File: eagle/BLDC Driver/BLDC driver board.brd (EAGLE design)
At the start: 59.7 x 47 mm, 25 parts, among them Q1 MOSFET-NCHANNEL, Q2 MOSFET-NCHANNEL, Q3 MOSFET-NCHANNEL, Q4 MOSFET-NCHANNEL, Q5 MOSFET-NCHANNEL, Q6 MOSFET-NCHANNEL, U2 AUIRS2334S

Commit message: Started working on new driver board.
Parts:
- removed D1, D2, D6: (no value), CMPE118lib:DIODE-HV
- removed U2: AUIRS2334S, ASL:SO20W
- added 5V: (no value), jumper:JP1
- added C5, C6, R2: (no value), ASL:0805
- added U$2: DRV8302, ASL:SOP63P1035X279-56N
- C1: value 470nF -> .1uF; device CMPE118lib:1206 -> ASL:0805
- C2: value 470nF -> 4.7uF; device CMPE118lib:1206 -> ASL:0805
- C3: value 470nF -> .015uF; device CMPE118lib:1206 -> ASL:0805
- C4: value 1uF -> (none); device CMPE118lib:1206 -> ASL:0805
- moved C4 80.9 mm to (-17.8, -30.5), turned to 0 degrees
- moved C3 70.8 mm to (-17.8, -20.3)
- moved C2 59.5 mm to (-17.8, -10.2)
- moved C1 52.6 mm to (-17.8, -5.08)
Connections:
- removed net N$11: C3.1, D6.C, U2.14
- new net CRRNTSNS1: U$1.P$21
- new net CRRNTSNS2: U$1.P$4
- new net N$1: C3.2, U$2.56
- new net N$4: C4.1, U$2.48
- new net N$5: C4.2, U$2.46
- new net N$6: C5.1, U$2.43
- new net N$8: C6.1, U$2.38
- new net N$9: C6.2, U$2.36
- new net PGND: Q2.3, Q4.3, Q6.3, U$2.P$1
- new net PVDD: C1.1, C2.1, Q1.4, Q1.4@1, Q1.P$2, Q1.P$3, Q1.P$4, Q1.P$5, Q1.P$6, Q1.P$7, Q1.P$8, Q1.P$9, Q3.4, Q3.4@1, Q3.P$2, Q3.P$3, Q3.P$4, Q3.P$5, Q3.P$6, Q3.P$7, Q3.P$8, Q3.P$9, Q5.4, Q5.4@1, Q5.P$2, Q5.P$3, Q5.P$4, Q5.P$5, Q5.P$6, Q5.P$7, Q5.P$8, Q5.P$9, U$2.29, U$2.53, U$2.54
- net +UB: no longer Q1.4, Q1.4@1, Q1.P$2, Q1.P$3, Q1.P$4, Q1.P$5, Q1.P$6, Q1.P$7, Q1.P$8, Q1.P$9, Q3.4, Q3.4@1, Q3.P$2, Q3.P$3, Q3.P$4, Q3.P$5, Q3.P$6, Q3.P$7, Q3.P$8, Q3.P$9, Q5.4, Q5.4@1, Q5.P$2, Q5.P$3, Q5.P$4, Q5.P$5, Q5.P$6, Q5.P$7, Q5.P$8, Q5.P$9
- net -UB: no longer Q2.3, Q4.3, Q6.3
- net GND: now also 5V.1, C1.2, C2.2, C3.1, R2.2; no longer C4.2, U2.7
- net HO1: no longer U2.19
- net HO2: no longer U2.16
- net HO3: no longer U2.13
- net LO1: no longer U2.10
- net LO2: no longer U2.9
- net LO3: no longer U2.8
- net N$3: now also R2.1, U$2.49; no longer C1.1, D1.C, U2.20
- net N$7: now also C5.2, U$2.41; no longer C2.1, D2.C, U2.17
- net OUTPUTA: no longer C1.2, U2.18
- net OUTPUTB: no longer C2.2, U2.15
- net OUTPUTC: no longer C3.2, U2.12
- net PWM1: now also U$2.17; no longer U2.1, U2.4
- net PWM2: now also U$2.19; no longer U2.2, U2.5
- net PWM3: now also U$2.21; no longer U2.3, U2.6
- net VCC: now also 5V.2; no longer C4.1, D1.A, D2.A, D6.A, U2.11
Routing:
- net OUTPUTB: track 159.1 -> 0.00 mm, vias 4 -> 0
- net OUTPUTA: track 134.1 -> 0.00 mm, vias 1 -> 0
- net HO2: track 115.8 -> 0.00 mm, vias 4 -> 0
- net OUTPUTC: track 100.6 -> 0.00 mm, vias 4 -> 0
- net LO3: track 86.0 -> 0.00 mm
- net LO1: track 75.3 -> 0.00 mm, vias 2 -> 0
- net LO2: track 65.8 -> 0.00 mm
- net VCC: track 65.3 -> 0.00 mm
- net PWM2: track 55.6 -> 0.00 mm, vias 3 -> 0
- net PWM3: track 54.0 -> 0.00 mm, vias 3 -> 0
- net PWM1: track 52.3 -> 0.00 mm, vias 1 -> 0
- net HO1: track 51.7 -> 0.00 mm, vias 2 -> 0
- net HO3: track 40.7 -> 0.00 mm, vias 2 -> 0
- net ADC/HALL1: track 34.9 -> 0.00 mm, vias 2 -> 0
- net N$11: track 27.5 -> 0.00 mm, vias 2 -> 0
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- removed copper zone on layer 1, net +UB
- removed copper zone on layer 16, net +UB
- removed copper zone on layer 1, net -UB
- removed copper zone on layer 16, net -UB
- removed copper zone on layer 1, net GND

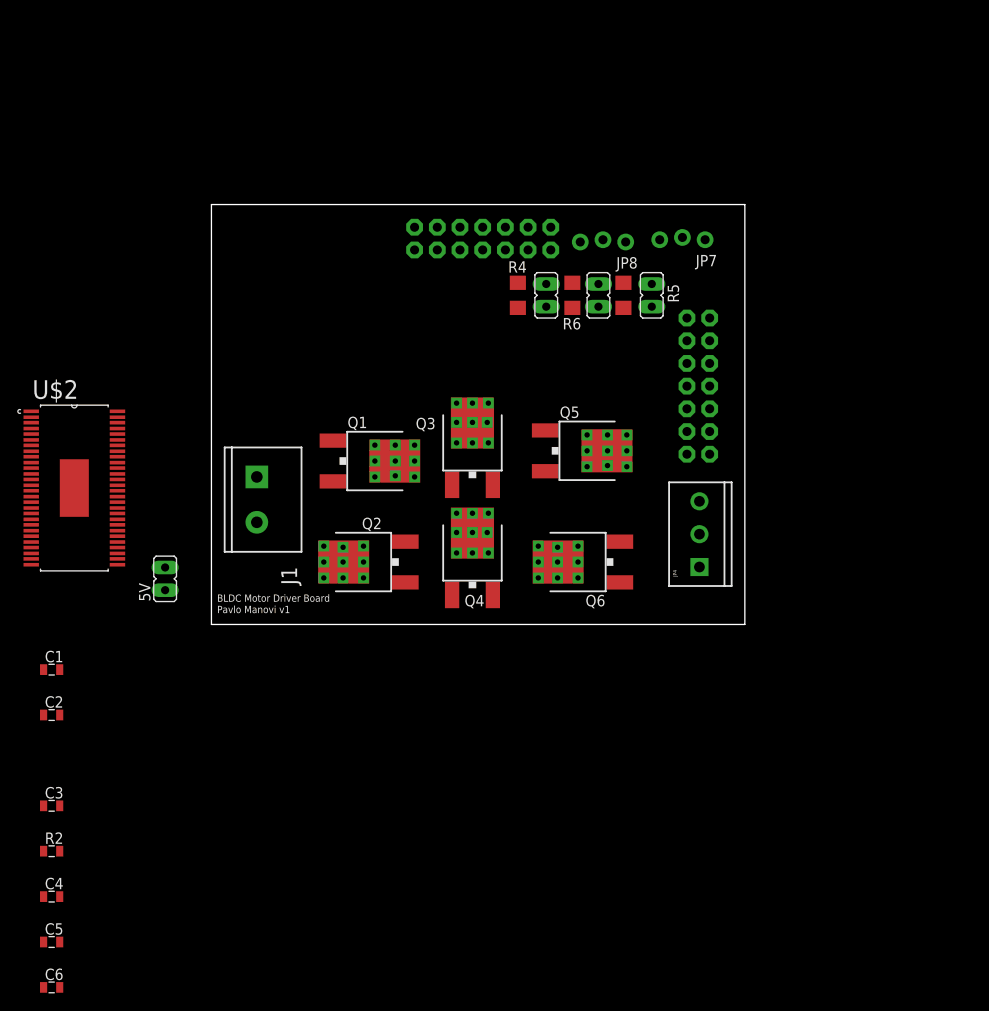
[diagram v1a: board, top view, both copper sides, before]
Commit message: Finished BLDC Driver v2.1
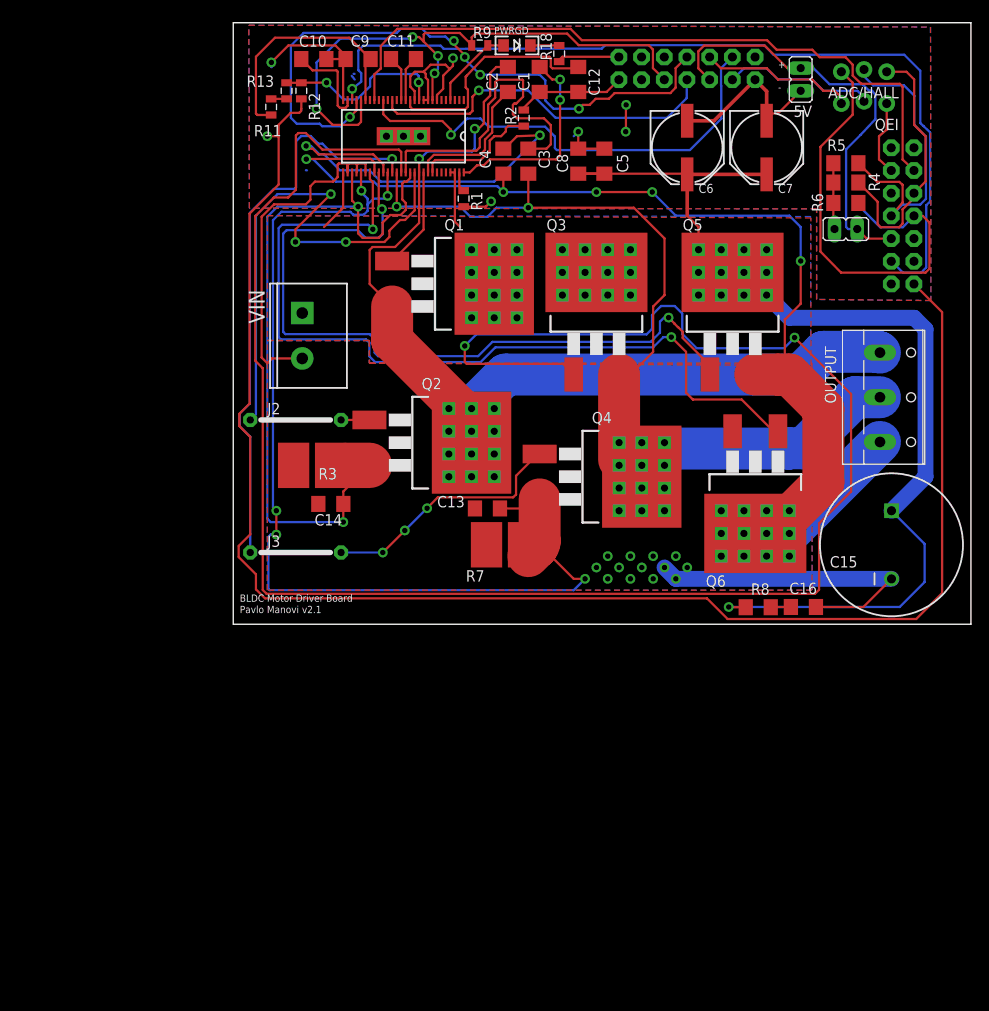
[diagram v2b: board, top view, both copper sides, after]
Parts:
- removed J1: (no value), CMPE118lib:SCREW_TERMINAL-5.08MM-2
- removed JP1, JP2: (no value), jumper:JP1
- removed JP4: (no value), CMPE118lib:SCREWTERMINAL-3.5MM-3_LOCK.007S
- removed JP7, JP8: (no value), CMPE118lib:1X03_LOCK_NO_SILK
- removed U$2: DRV8302, ASL:SOP63P1035X279-56N
- added ADC/HALL, QEI: (no value), CMPE118lib:1X03_LOCK_NO_SILK
- added C10, C9: 1uF, ASL:1206
- added C11: 22nF, ASL:1206
- added C12: 2.2uF, ASL:1206
- added C13, C14: 1nF, ASL:1206
- added C15: 470, ASL:CPOL-RADIAL-1000UF-63V
- added C16: 10nF, ASL:1206
- added C7: 4.7uF, ASL:PANASONIC_E
- added C8: .1uF, ASL:1206
- added DRV8301: DRV8302, ASL:HTSSOP56
- added J2, J3: J10MM, jumper:10
- added LED3: (no value), ASL:LED-1206
- added OUTPUT: (no value), con-wago-500:W237-103
- added R1, R11, R9: 10k, ASL:0805
- added R12: 3.16, ASL:0805
- added R13: 470, ASL:0805
- added R18: 330, ASL:0805
- added R3, R7: .01, ASL:SMT-REF
- added R8: 3.3, CMPE118lib:1206
- added VIN: (no value), CMPE118lib:SCREW_TERMINAL-5.08MM-2
- C1: value .1uF -> .015uF; device ASL:0805 -> ASL:1206
- C2: value 4.7uF -> .1uF; device ASL:0805 -> ASL:1206
- C3: value .015uF -> .1uF; device ASL:0805 -> ASL:1206
- C4, C5: value (none) -> .1uF; device ASL:0805 -> ASL:1206
- C6: value (none) -> 47uF; device ASL:0805 -> ASL:PANASONIC_E
- Q1, Q2, Q3, Q4, Q5, Q6: value MOSFET-NCHANNEL -> FDB86135; device ASL:DPAK-VIA -> ASL:D2PACK
- R2: value (none) -> 1M
- moved C6 117.9 mm to (53.3, 53.3), turned to 270 degrees
- moved C5 107.1 mm to (44.1, 51.8), turned to 90 degrees
- moved R2 97.6 mm to (35.1, 56.6), turned to 90 degrees
- moved C4 96.6 mm to (32.8, 51.8), turned to 270 degrees
- moved 5V 90.4 mm to (66.0, 61.0)
- moved C3 89.7 mm to (35.6, 51.8), turned to 270 degrees
- moved C2 87.5 mm to (33.3, 61.0), turned to 90 degrees
- moved C1 85.7 mm to (36.8, 61.0), turned to 90 degrees
- moved R4 38.8 mm to (71.1, 49.4), turned to 180 degrees
- moved R6 32.3 mm to (71.1, 47.1), turned to 180 degrees
- moved U$1 29.8 mm to (31.2, 29.8)
- moved R5 29.0 mm to (71.1, 51.6), turned to 180 degrees
- moved JP3 28.7 mm to (71.1, 44.2), turned to 270 degrees
- moved Q5 23.4 mm to (58.4, 36.8), turned to 0 degrees
- moved Q1 22.3 mm to (29.2, 38.1)
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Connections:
- removed net +UB: J1.1
- removed net -UB: J1.2
- removed net HO1: Q1.1
- removed net HO2: Q3.1
- removed net HO3: Q5.1
- removed net LO1: Q2.1
- removed net LO2: Q4.1
- removed net LO3: Q6.1
- removed net N$26: JP1.1, R4.2
- removed net N$27: JP2.1, R5.2
- removed net N$28: JP3.1, R6.2
- removed net PGND: Q2.3, Q4.3, Q6.3, U$2.P$1
- removed net PVDD: C1.1, C2.1, Q1.4, Q1.4@1, Q1.P$2, Q1.P$3, Q1.P$4, Q1.P$5, Q1.P$6, Q1.P$7, Q1.P$8, Q1.P$9, Q3.4, Q3.4@1, Q3.P$2, Q3.P$3, Q3.P$4, Q3.P$5, Q3.P$6, Q3.P$7, Q3.P$8, Q3.P$9, Q5.4, Q5.4@1, Q5.P$2, Q5.P$3, Q5.P$4, Q5.P$5, Q5.P$6, Q5.P$7, Q5.P$8, Q5.P$9, U$2.29, U$2.53, U$2.54
- new net 3V3: DRV8301.16, DRV8301.24, DRV8301.8, R9.1, U$1.P$10, U$1.P$24
- new net GH_A: DRV8301.47, Q1.1
- new net GH_B: DRV8301.42, Q3.1
- new net GH_C: DRV8301.37, Q5.1
- new net GL_A: DRV8301.45, J2.1
- new net GL_B: DRV8301.40, J3.1
- new net GL_C: DRV8301.35, Q6.1
- new net N$10: DRV8301.55, R1.1
- new net N$11: DRV8301.4, LED3.A, R9.2
- new net N$12: DRV8301.11, R12.1, R13.2
- new net N$13: JP3.1, R4.2, R5.2, R6.2
- new net N$15: LED3.C, R18.2
- new net N$16: C10.1, DRV8301.27
- new net N$18: C9.1, DRV8301.23, R11.2
- new net N$19: C11.1, DRV8301.14
- new net N$20: C11.2, DRV8301.15
- new net N$21: C12.1, DRV8301.13
- new net SN1: C13.1, DRV8301.33, DRV8301.39, Q4.3, R7.2
- new net SN2: C14.1, DRV8301.31, DRV8301.44, Q2.3, R3.2
- new net VNEG: C13.2, C14.2, C15.2, C16.2, DRV8301.30, DRV8301.32, DRV8301.34, Q6.3, R3.1, R7.1, VIN.2
- new net V_BATT: C15.1, C5.1, C6.+, C7.+, C8.1, DRV8301.29, DRV8301.53, DRV8301.54, Q1.2, Q1.P$1, Q1.P$10, Q1.P$11, Q1.P$12, Q1.P$2, Q1.P$3, Q1.P$4, Q1.P$5, Q1.P$6, Q1.P$7, Q1.P$8, Q1.P$9, Q3.2, Q3.P$1, Q3.P$10, Q3.P$11, Q3.P$12, Q3.P$2, Q3.P$3, Q3.P$4, Q3.P$5, Q3.P$6, Q3.P$7, Q3.P$8, Q3.P$9, Q5.2, Q5.P$1, Q5.P$10, Q5.P$11, Q5.P$12, Q5.P$2, Q5.P$3, Q5.P$4, Q5.P$5, Q5.P$6, Q5.P$7, Q5.P$8, Q5.P$9, R8.2, VIN.1
- net ADC/HALL1: now also ADC/HALL.3, R6.1; no longer JP1.2, JP8.3
- net ADC/HALL2: now also ADC/HALL.2, R5.1; no longer JP2.2, JP8.2
- net ADC/HALL3: now also ADC/HALL.1, R4.1; no longer JP3.2, JP8.1
- net CRRNTSNS1: now also DRV8301.25
- net CRRNTSNS2: now also DRV8301.26
- net GND: now also C1.1, C10.2, C12.2, C5.2, C6.-, C7.-, C8.2, C9.2, DRV8301.10, DRV8301.12, DRV8301.28, DRV8301.57, DRV8301.7, DRV8301.9, DRV8301.P$1, DRV8301.P$2, DRV8301.P$3, R1.2, R13.1, R18.1; no longer C1.2, C2.2, C3.1
- net N$1: now also C1.2, DRV8301.56; no longer C3.2, U$2.56
- net N$2: now also J2.2, Q2.1; no longer U$1.P$24
- net N$3: now also DRV8301.49; no longer U$2.49
- net N$4: now also C2.1, DRV8301.48; no longer C4.1, U$2.48
- net N$5: now also J3.2, Q4.1; no longer C4.2, U$2.46
- net N$6: now also C3.1, DRV8301.43; no longer C5.1, U$2.43
- net N$7: now also C16.1, R8.1; no longer C5.2, U$2.41
- net N$8: now also C4.1, DRV8301.38; no longer C6.1, U$2.38
- net N$9: now also R11.1, R12.2; no longer C6.2, U$2.36
- net OUTPUTA: now also C2.2, DRV8301.46, OUTPUT.1, Q2.2, Q2.P$1, Q2.P$10, Q2.P$11, Q2.P$12; no longer JP4.1, Q2.4, Q2.4@1
- net OUTPUTB: now also C3.2, DRV8301.41, OUTPUT.2, Q4.2, Q4.P$1, Q4.P$10, Q4.P$11, Q4.P$12; no longer JP4.2, Q4.4, Q4.4@1
- net OUTPUTC: now also C4.2, DRV8301.36, OUTPUT.3, Q6.2, Q6.P$1, Q6.P$10, Q6.P$11, Q6.P$12; no longer JP4.3, Q6.4, Q6.4@1
- net PWM1: now also DRV8301.17; no longer U$2.17
- net PWM2: now also DRV8301.19; no longer U$2.19
- net PWM3: now also DRV8301.21; no longer U$2.21
- net QEI-A: now also QEI.3; no longer JP7.3
- net QEI-B: now also QEI.2; no longer JP7.2
- net QEI-INDEX: now also QEI.1; no longer JP7.1
- net VCC: now also JP3.2; no longer R4.1, R5.1, R6.1
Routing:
- net GND: track 0.00 -> 263.3 mm, vias 0 -> 7
- net GH_B: track 0.00 -> 222.1 mm, vias 0 -> 2
- net OUTPUTC: track 0.00 -> 130.0 mm, vias 0 -> 5
- net V_BATT: track 0.00 -> 126.0 mm, vias 0 -> 1
- net SN1: track 0.00 -> 119.4 mm, vias 0 -> 5
- net OUTPUTA: track 0.00 -> 106.2 mm, vias 0 -> 2
- net CRRNTSNS2: track 0.00 -> 98.2 mm, vias 0 -> 1
- net OUTPUTB: track 0.00 -> 97.9 mm, vias 0 -> 2
- net GL_C: track 0.00 -> 95.7 mm, vias 0 -> 2
- net GH_C: track 0.00 -> 86.0 mm, vias 0 -> 2
- net SN2: track 0.00 -> 84.5 mm, vias 0 -> 2
- net PWM3: track 0.00 -> 78.9 mm
- net VNEG: track 0.00 -> 76.1 mm, vias 0 -> 13
- net CRRNTSNS1: track 0.00 -> 72.0 mm, vias 0 -> 5
- net 3V3: track 0.00 -> 67.2 mm, vias 0 -> 4
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- added copper zone on layer 1, net GND
- added copper zone on layer 16, net GND
- added copper zone on layer 16, net OUTPUTA
- added copper zone on layer 16, net OUTPUTB
- added copper zone on layer 16, net OUTPUTC
- added copper zone on layer 1, net VNEG
- added copper zone on layer 16, net VNEG
- added copper zone on layer 1, net V_BATT
- added copper zone on layer 16, net V_BATT
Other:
- board size 59.7 x 47 mm -> 82.5 x 67.3 mm
- board text added: "+"
- board text added: "-"
- board text added: "PWRGD"
- board text added: "Pavlo Manovi v2.1"
- board text removed: "Pavlo Manovi v1"

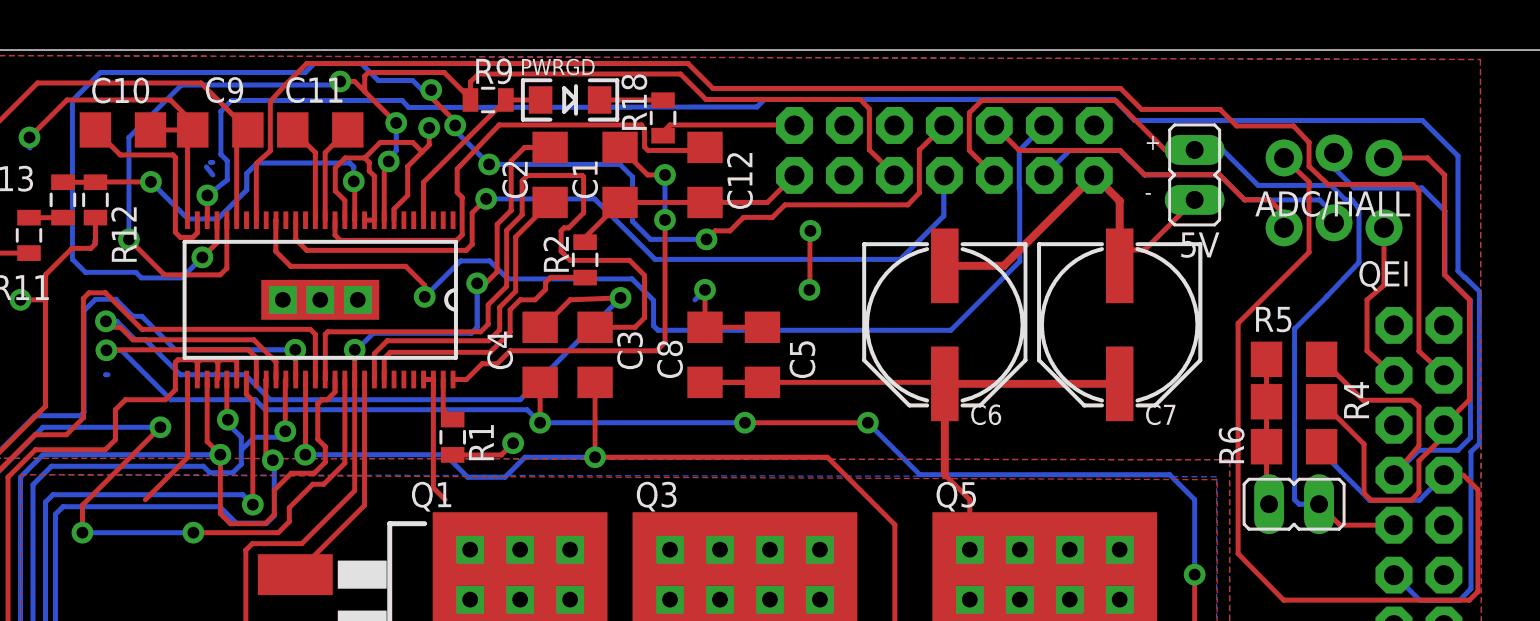
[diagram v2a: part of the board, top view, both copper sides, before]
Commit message: Finished v 2 of the BLDC driver board
Finished the alumni board

Finished the MAC.PHY_shield for the ASL CAN node.

Signed-off-by: Pavlo Manovi <pavlo.manovi@gmail.com>
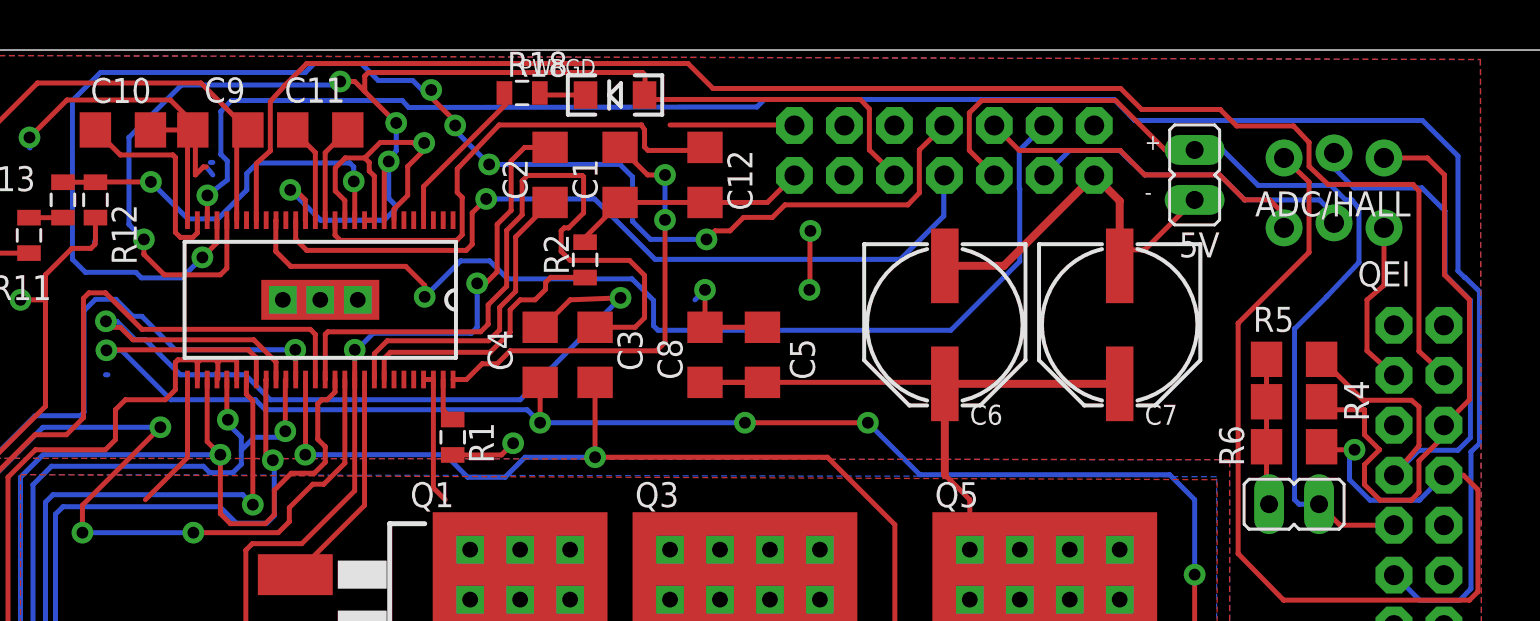
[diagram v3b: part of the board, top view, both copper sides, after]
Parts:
- removed R9: 10k, ASL:0805
- R12: value 3.16 -> 3.16k
- moved R18 7.27 mm to (31.9, 65.1), turned to 0 degrees
- moved LED3 2.30 mm to (36.6, 65.0), turned to 180 degrees
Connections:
- net 3V3: now also LED3.A; no longer R9.1
- net GND: no longer R18.1
- net N$11: now also R18.1; no longer LED3.A, R9.2
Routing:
- net 3V3: track 67.2 -> 76.9 mm, vias 4 -> 5
- net GND: track 263.3 -> 265.4 mm
- net N$11: track 9.61 -> 8.20 mm
- net ADC/HALL3: track 29.8 -> 31.2 mm
- net ADC/HALL1: track 50.9 -> 52.0 mm, vias 0 -> 1
- net N$15: track 3.23 -> 2.37 mm
